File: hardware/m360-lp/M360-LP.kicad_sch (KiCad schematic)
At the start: 57 parts, among them J1 RJ45 SOLO, J2 RJ45 CLIMA/AUX, J3 J_VIN 3,0-6V, J4 M360-RF, Q1 AO3401A, Q2 AO3401A, SW1 Reed, U1 MCP1700T-3302E/TT, U2 74HC4051, U3 SRV05-4, U4 SRV05-4, U5 SRV05-4

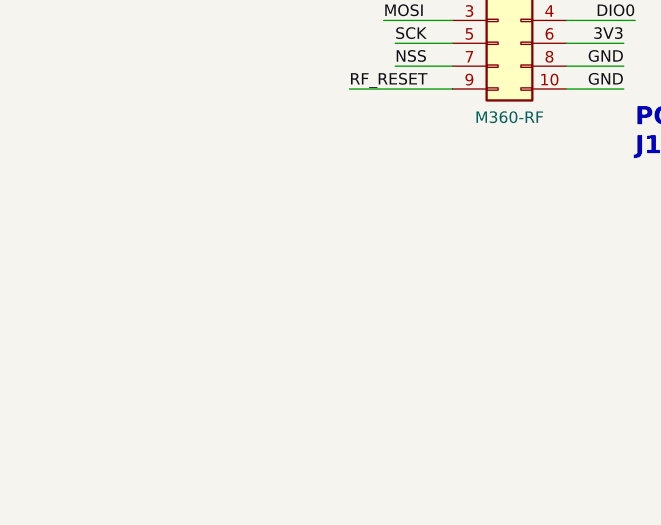
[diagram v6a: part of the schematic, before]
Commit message: feat(hardware): header 1x8 do nRF24 legado nas placas GW, LP e ACT
- esquemáticos: header 1x8 "nRF24 legado" (GW J4, LP J5, ACT J6; C492407,
  solda manual, fora do BOM e da posição) e 10 uF 0805 (C5/C16/C9, C15850)
  nas mesmas redes do soquete do mezanino: CE = DIO0, CSN = NSS, IRQ = DIO1
  (sem ligação na GW). Um rádio por placa: nRF24 OU mezanino RFM95W
- tools/add_nrf_header.py: grava símbolo, fios e labels por texto, embute o
  Conn_01x08 stock e confere colisão; netdiff só nas redes previstas, ERC 0,
  campos e lib_symbols inalterados nas três folhas
- placas rerroteadas sem apagar a fiação existente (DSN com fios fixos e
  cobertos por área proibida, mais áreas proibidas sobre os fiduciais);
  vias de GND junto do pino 8 e do capacitor; legenda "nRF24 OU mezanino"
  e "CE" no pino 1. GW 287 trilhas/43 vias, LP 855/135, ACT 939/141;
  DRC --severity-all 0/0, paridade idêntica, ordem_tvs 13/13 e 15/15
- fabricacao/ regerada: GW 15, LP 53, ACT 54 peças
- ARQUITETURA §2 (decisão 15), §4.2, §5.2, §6.1, §8, §9, §9.1; datasheet
  C492407 em docs/datasheets. Firmware pendente: MY_RF24_CE_PIN=5 (GW) e
  =2 (LP/ACT), a testar na bancada

Co-Authored-By: Claude Fable 5.1 <noreply@anthropic.com>
Claude-Session: https://claude.ai/code/session_01M8U92DFNnZt7SqLtzrKYSR
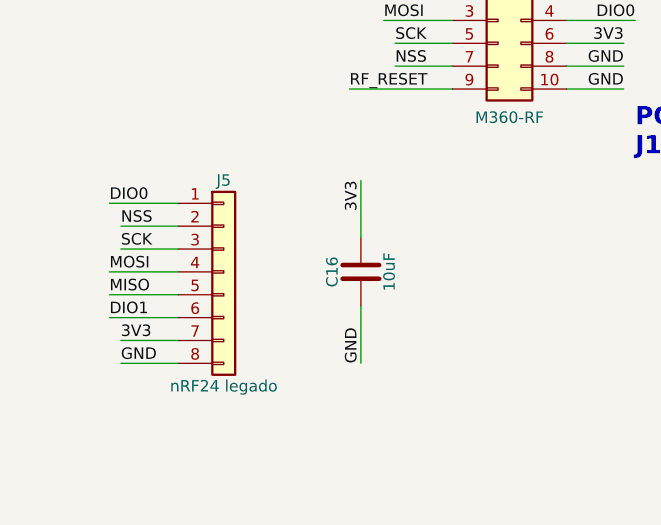
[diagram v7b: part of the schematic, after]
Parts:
- added C16: 10uF, Capacitor_SMD:C_0805_2012Metric, symbol Device:C
- added J5: nRF24 legado, Connector_PinHeader_2.54mm:PinHeader_1x08_P2.54mm_Vertical, symbol Connector_Generic:Conn_01x08
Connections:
- net 3V3: now also C16.1, J5.7 (Pin_7)
- net DIO0: now also J5.1 (Pin_1)
- net DIO1: now also J5.6 (Pin_6)
- net GND: now also C16.2, J5.8 (Pin_8)
- net MISO: now also J5.5 (Pin_5)
- net MOSI: now also J5.4 (Pin_4)
- net NSS: now also J5.2 (Pin_2)
- net SCK: now also J5.3 (Pin_3)
